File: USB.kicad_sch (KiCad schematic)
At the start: 8 parts, among them J3 USB-C_GCT_USB4145-03-0070-C, U11 TPD4E05U06QDQARQ1

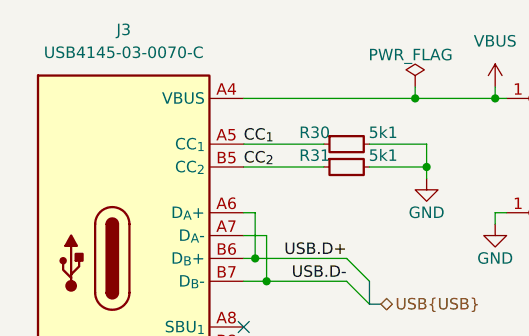
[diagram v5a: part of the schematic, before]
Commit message: [#72133] Change connectors to horizontal
Signed-off-by: Dawid Lentka <dlentka@antmicro.com>
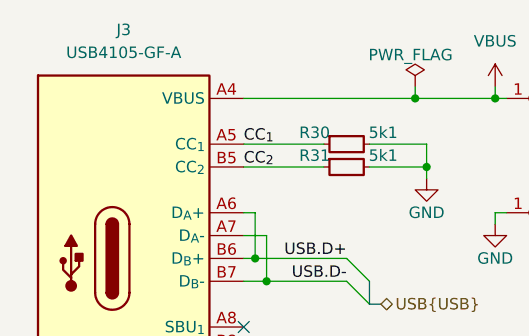
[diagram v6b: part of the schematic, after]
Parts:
- J3: value USB-C_GCT_USB4145-03-0070-C -> USB-C_GCT_USB4105-GF-A; footprint antmicro-footprints:USB-C_Receptacle_GCT_USB4145-03-0070-C -> antmicro-footprints:USB-C_Receptacle_GCT_USB4105-GF-A; symbol antmicroUSBConnectors:USB-C_GCT_USB4145-03-0070-C -> antmicroUSBConnectors:USB-C_GCT_USB4105-GF-A; MPN USB4145-03-0070-C -> USB4105-GF-A
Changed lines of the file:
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@@
 	)
 	(symbol
-		(lib_id "antmicroUSBConnectors:USB-C_GCT_USB4145-03-0070-C")
+		(lib_id "antmicroUSBConnectors:USB-C_GCT_USB4105-GF-A")
 		(at 149.86 74.93 0)
 		(unit 1)
@@
 			)
 		)
-		(property "Value" "USB-C_GCT_USB4145-03-0070-C"
-			(at 171.45 82.55 0)
+		(property "Value" "USB-C_GCT_USB4105-GF-A"
+			(at 136.525 69.85 0)
 			(effects
 				(font
@@
 					(thickness 0.15)
 				)
-				(justify left bottom)
 				(hide yes)
 			)
 		)
-		(property "Footprint" "antmicro-footprints:USB-C_Receptacle_GCT_USB4145-03-0070-C"
+		(property "Footprint" "antmicro-footprints:USB-C_Receptacle_GCT_USB4105-GF-A"
 			(at 171.45 85.09 0)
 			(effects
@@
 			)
 		)
-		(property "Datasheet" "https://gct.co/files/drawings/usb4145.pdf"
+		(property "Datasheet" "https://gct.co/files/drawings/usb4105.pdf"
 			(at 171.45 87.63 0)
 			(effects
@@
 			)
 		)
-		(property "Description" "USB-C (USB TYPE-C) USB 2.0 Receptacle Connector 24 (16+8 Dummy) Postion  Surface Mount, Vertical"
+		(property "Description" "USB-C (USB TYPE-C) USB 2.0 Receptacle Connector 24 (16+8 Dummy) Position Surface Mount, Right Angle"
 			(at 149.86 74.93 0)
 			(effects
@@
 			)
 		)
-		(property "MPN" "USB4145-03-0070-C"
+		(property "MPN" "USB4105-GF-A"
 			(at 136.525 69.85 0)
 			(effects

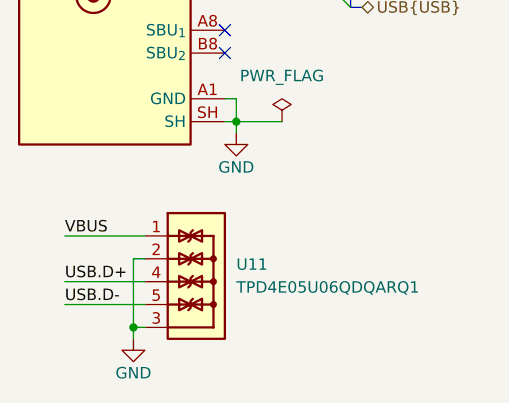
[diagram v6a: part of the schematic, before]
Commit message: [#72133] Sch: Add IMU
Signed-off-by: Dawid Lentka <dlentka@antmicro.com>
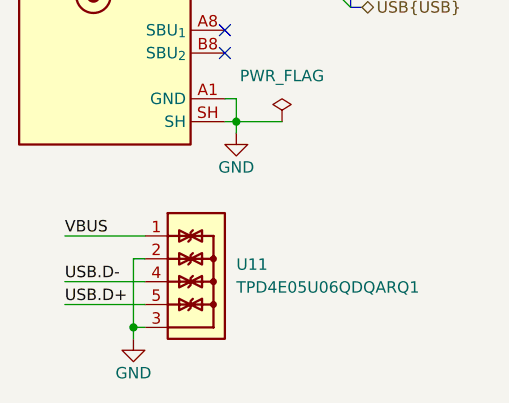
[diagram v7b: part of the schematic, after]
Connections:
- net USB.D+: now also U11.5, U11.6; no longer U11.4, U11.7
- net USB.D-: now also U11.4, U11.7; no longer U11.5, U11.6
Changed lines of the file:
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@@
 	)
 	(label "USB.D+"
-		(at 132.08 128.27 0)
+		(at 132.08 130.81 0)
 		(fields_autoplaced yes)
 		(effects
@@
 	)
 	(label "USB.D-"
-		(at 132.08 130.81 0)
+		(at 132.08 128.27 0)
 		(fields_autoplaced yes)
 		(effects

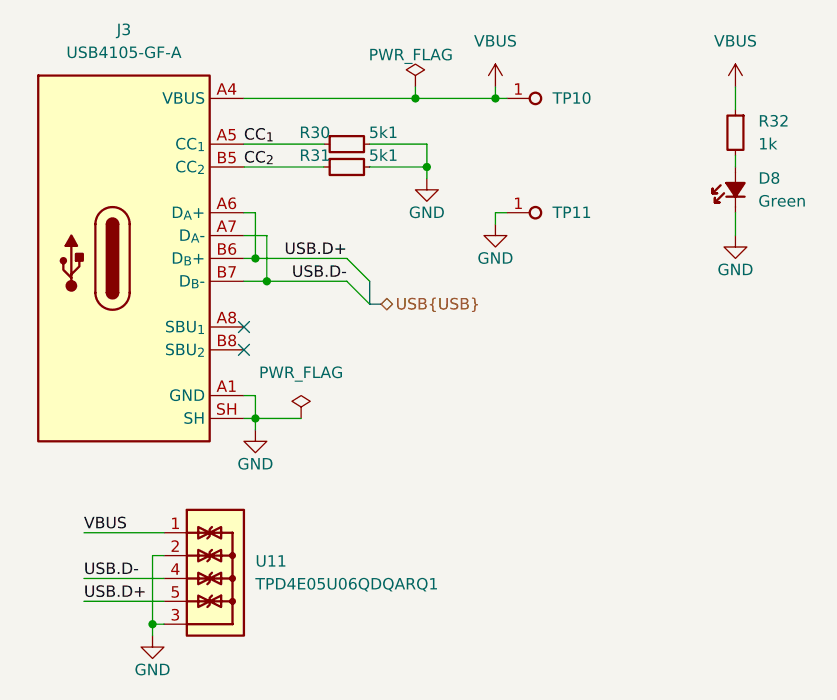
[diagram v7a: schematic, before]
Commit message: [#72133] Sch: Update control hierarchy
Signed-off-by: Dawid Lentka <dlentka@antmicro.com>
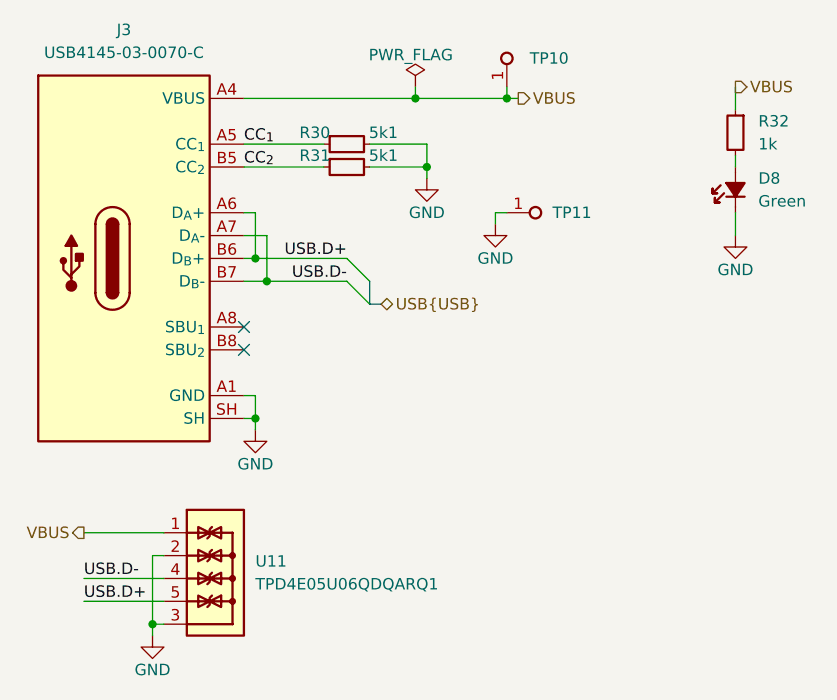
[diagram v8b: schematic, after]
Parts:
- J3: value USB-C_GCT_USB4105-GF-A -> USB-C_GCT_USB4145-03-0070-C; footprint antmicro-footprints:USB-C_Receptacle_GCT_USB4105-GF-A -> antmicro-footprints:USB-C_Receptacle_GCT_USB4145-03-0070-C; symbol antmicroUSBConnectors:USB-C_GCT_USB4105-GF-A -> antmicroUSBConnectors:USB-C_GCT_USB4145-03-0070-C; MPN USB4105-GF-A -> USB4145-03-0070-C
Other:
- moved on the sheet: TP10
